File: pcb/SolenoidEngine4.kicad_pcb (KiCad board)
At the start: 4 copper layers, 208 x 118 mm, 119 parts, among them IC1 TPS2819DBVT, IC2 STM32C092FCP6, IC3 TPS2819DBVT, IC4 TPS2819DBVT, IC5 TPS2819DBVT, IC6 TPS2819DBVT, IC7 LDL1117S33R, J10 Screw_Terminal_01x02, J12 Screw_Terminal_01x02, J13 Screw_Terminal_01x02, J14 Screw_Terminal_01x02, J15 TB005-762-02BE, J16 TB005-762-02BE, J17 TB005-762-02BE, J18 TB005-762-02BE, J3 Screw_Terminal_01x02, J7 Screw_Terminal_01x02, Q1 STH315N10F7-2, Q2 STH315N10F7-2, Q3 STH315N10F7-2, Q4 STH315N10F7-2, Q5 STH315N10F7-2, U1 STLINK-V3MODS

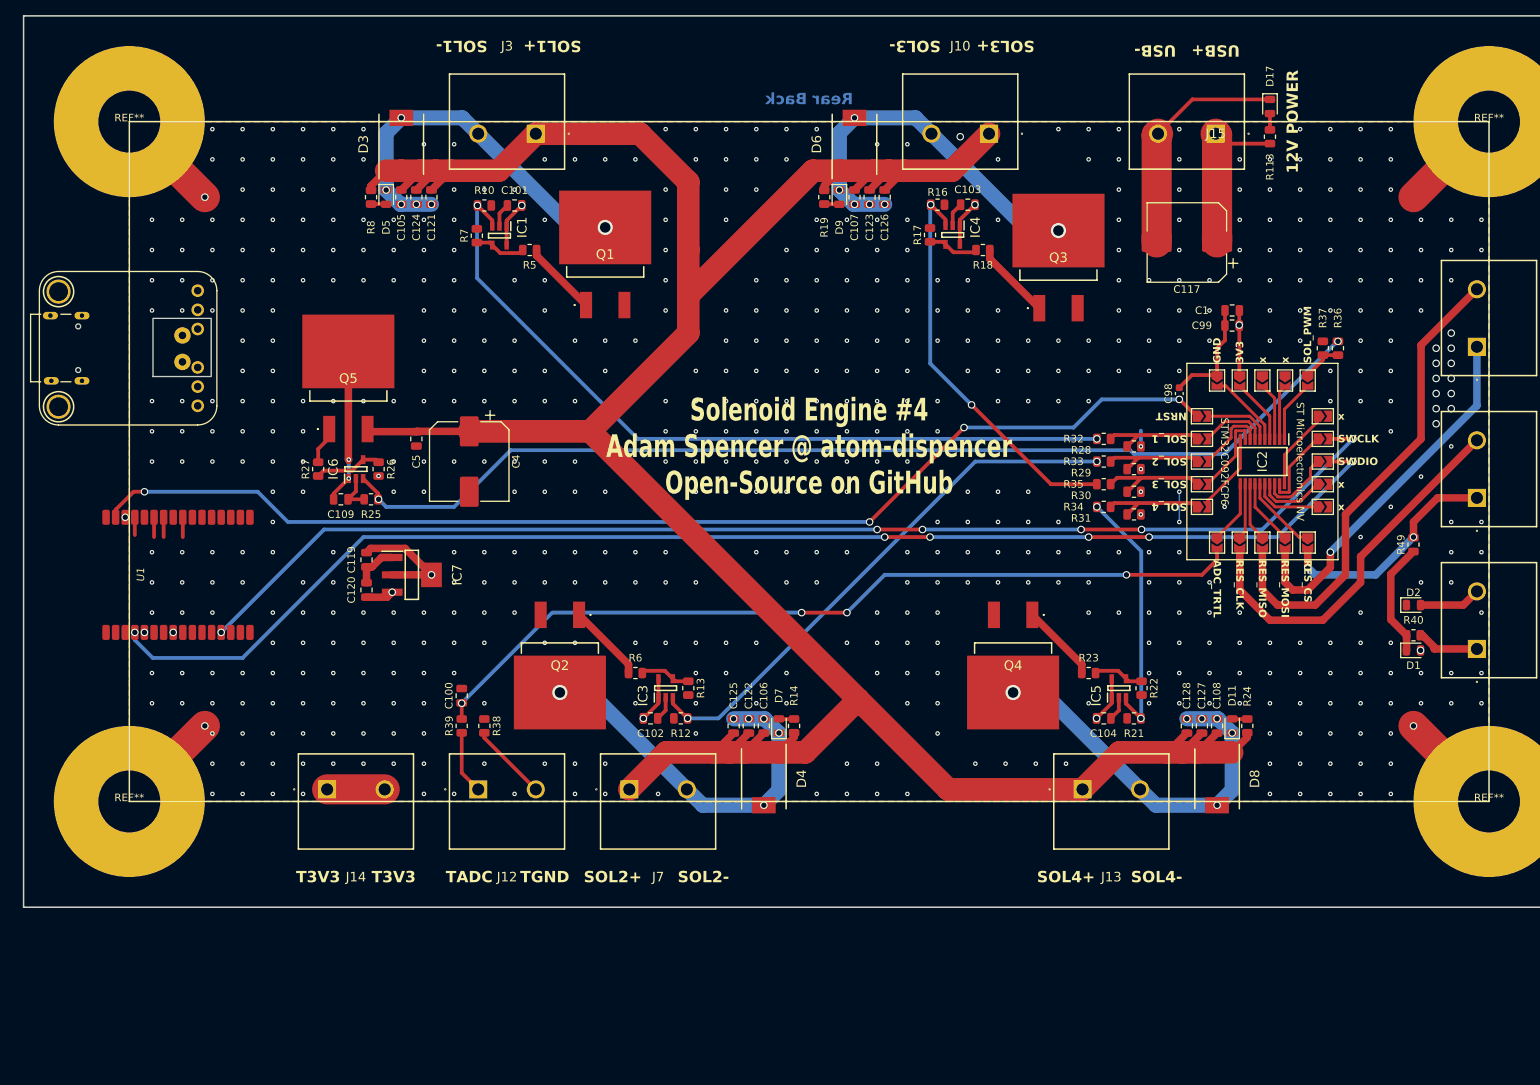
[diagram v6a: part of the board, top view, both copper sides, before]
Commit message: I forgot to put the holes in
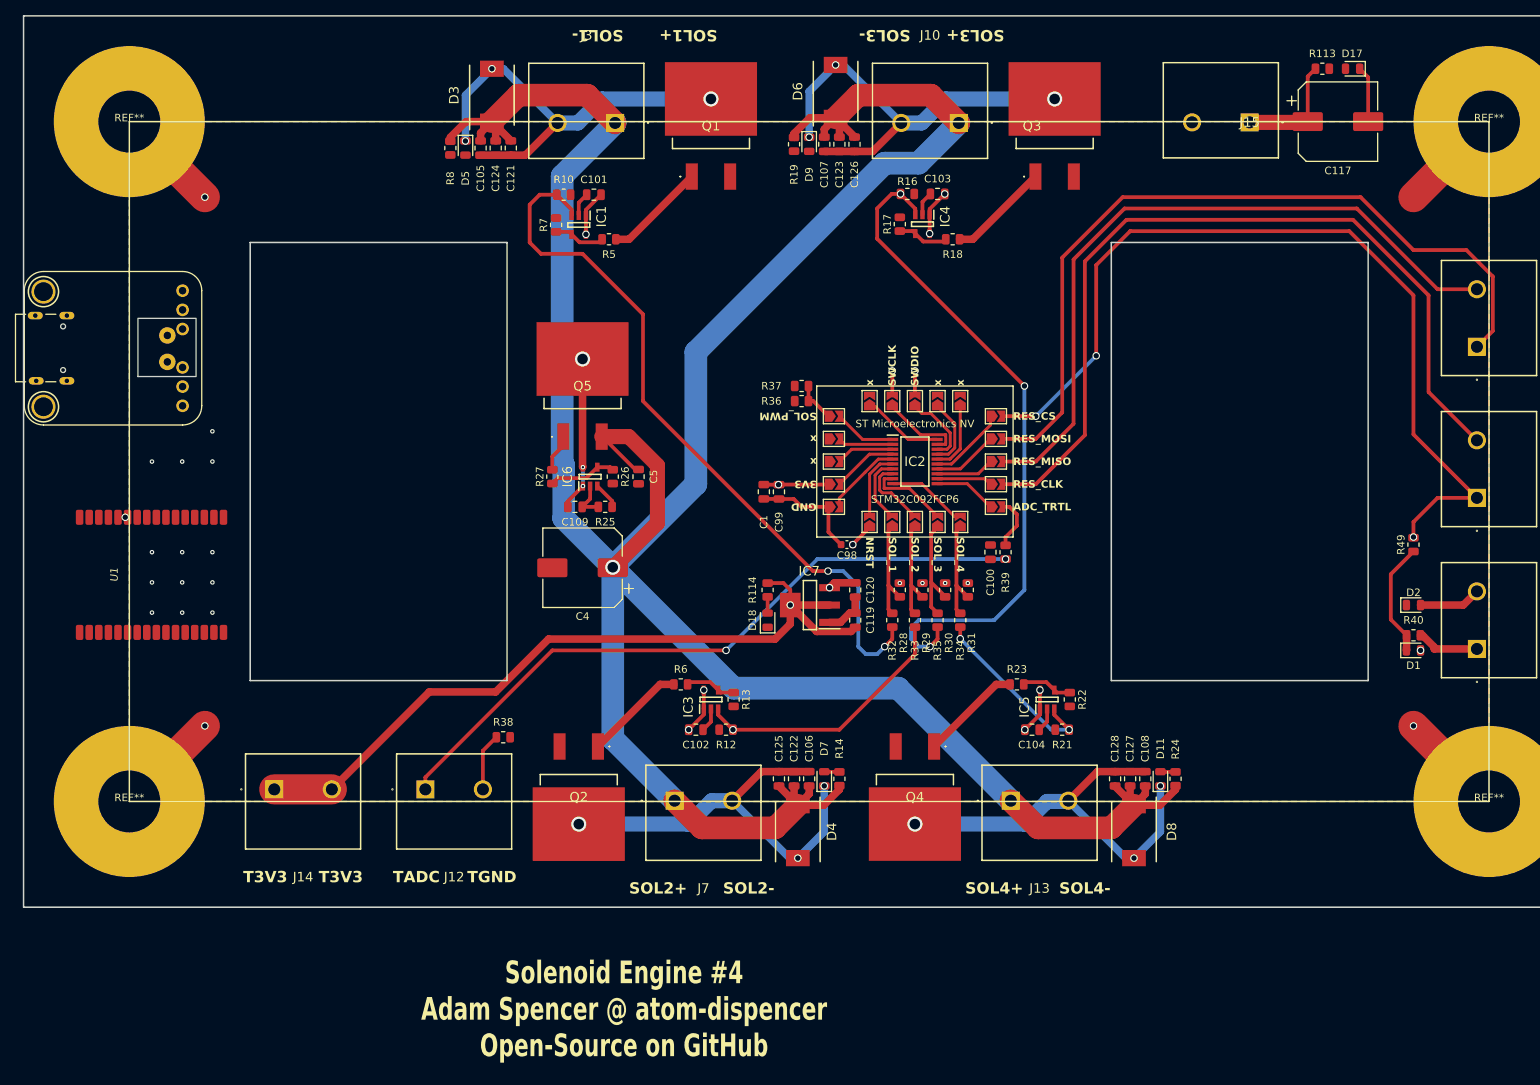
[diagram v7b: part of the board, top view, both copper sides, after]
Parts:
- added D18: LED, Diode_SMD:D_0805_2012Metric, F.Cu at (134.5, 116.0)
- added R114: 4k7, Resistor_SMD:R_0805_2012Metric, F.Cu at (134.5, 112.0)
- moved R39 75.6 mm to (166.0, 107.0)
- moved C100 72.5 mm to (164.0, 107.0), turned to -90 degrees
- moved R36 71.3 mm to (139.0, 87.0), turned to 0 degrees
- moved R37 69.2 mm to (139.0, 85.0), turned to 0 degrees
- moved C1 66.5 mm to (134.0, 99.0), turned to -90 degrees
- moved C119 65.2 mm to (146.1, 116.0), turned to 90 degrees
- moved C120 64.7 mm to (146.1, 112.0), turned to -90 degrees
- moved C99 63.9 mm to (136.0, 99.0), turned to -90 degrees
- moved JP11 62.9 mm to (143.3, 89.0), turned to 0 degrees
- moved JP12 60.2 mm to (143.3, 92.0), turned to 0 degrees
- moved JP1 60.0 mm to (148.0, 87.0), turned to 90 degrees
- moved JP13 57.7 mm to (143.3, 95.0), turned to 0 degrees
- moved JP2 57.2 mm to (151.0, 87.0), turned to 90 degrees
- moved JP14 55.5 mm to (143.3, 98.0), turned to 0 degrees
- moved JP3 54.6 mm to (154.0, 87.0), turned to 90 degrees
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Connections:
- C117 pad 1: /Power/12V_USB -> +12V
- J15 pad 1: /Power/12V_USB -> +12V
- R113 pad 1: /Power/12V_USB -> +12V
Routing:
- net /Microcontroller/SWDIO: track 177.3 -> 3.27 mm, vias 6 -> 1
- net /Microcontroller/SWCLK: track 163.7 -> 3.27 mm, vias 6 -> 1
- net /Microcontroller/NRST: track 154.4 -> 3.20 mm, vias 4 -> 1
- net /Microcontroller/SOL_PWM: track 140.5 -> 3.56 mm, vias 2 -> 0
- net /Microcontroller/MCU_ENG_THROTTLE: track 111.6 -> 7.17 mm, vias 4 -> 0
- net /Microcontroller/MCU_RESOLVER_CS: track 30.6 -> 117.3 mm, vias 2 -> 3
- net /Microcontroller/TRTL_ADC: track 8.39 -> 90.4 mm, vias 0 -> 2
- net +3V3: track 39.8 -> 117.4 mm
- net /Microcontroller/MCU_RESOLVER_CLK: track 50.2 -> 110.5 mm
- net /Solenoids/Solenoid 1/SOL+: track 360.2 -> 418.3 mm, vias 0 -> 1
- net /Microcontroller/MCU_RESOLVER_MOSI: track 49.2 -> 104.8 mm, vias 1 -> 0
- net GND: track 142.8 -> 102.8 mm, vias 598 -> 20
- net /Microcontroller/SOL_EN_3: track 53.3 -> 90.6 mm, vias 2 -> 3
- net /Microcontroller/SOL_EN_2: track 71.8 -> 35.4 mm, vias 2 -> 1
- net /Microcontroller/MCU_RESOLVER_MISO: track 63.8 -> 94.0 mm
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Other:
- outline, holes or cut-outs redrawn
- board text removed: "12V POWER"
- board text removed: "USB+"
- board text removed: "USB-"

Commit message: Fix .gitignore
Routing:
- net /Microcontroller/SWDIO: track 3.27 -> 145.0 mm, vias 1 -> 4
- net /Microcontroller/SWCLK: track 3.27 -> 129.0 mm, vias 1 -> 4
- net /Microcontroller/SOL_PWM: track 3.56 -> 41.2 mm, vias 0 -> 3
- net GND: track 102.8 -> 120.9 mm, vias 20 -> 8
- net Net-(D17-A): track 0.00 -> 2.15 mm
- net Net-(D9-A): track 0.00 -> 2.01 mm
- net Net-(D5-A): track 0.00 -> 2.01 mm
